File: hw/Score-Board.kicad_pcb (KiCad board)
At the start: 2 copper layers, 0 parts

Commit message: PCB routing done
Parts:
- added 5V: Conn_01x01, Connector_PinHeader_2.54mm:PinHeader_1x01_P2.54mm_Vertical, F.Cu at (151.0, 80.0)
- added BZ1: Buzzer, Buzzer_Beeper:Buzzer_12x9.5RM7.6, F.Cu at (133.2, 77.5)
- added C1: 10uF, Capacitor_THT:CP_Radial_D8.0mm_P3.50mm, F.Cu at (106.5, 113.1)
- added C2: 1.0uF, Capacitor_THT:CP_Radial_D5.0mm_P2.00mm, F.Cu at (140.3, 72.4)
- added C3: 1.0uF, Capacitor_THT:CP_Radial_D5.0mm_P2.00mm, F.Cu at (148.5, 72.4)
- added C4: 0.1uF, Capacitor_THT:CP_Radial_D5.0mm_P2.00mm, F.Cu at (217.8, 54.6)
- added C5: 0.1uF, Capacitor_THT:CP_Radial_D5.0mm_P2.00mm, F.Cu at (46.4, 54.6)
- added D1: 1N4004, Diode_THT:D_DO-41_SOD81_P10.16mm_Horizontal, F.Cu at (123.1, 90.2)
- added D2: D_Schottky_PP, Diode_THT:D_DO-35_SOD27_P10.16mm_Horizontal, F.Cu at (138.3, 90.2)
- added D3: D_Schottky, Diode_THT:D_DO-35_SOD27_P10.16mm_Horizontal, F.Cu at (130.7, 90.2)
- added D4: D_Schottky_PP, Diode_THT:D_DO-35_SOD27_P10.16mm_Horizontal, F.Cu at (146.0, 90.2)
- added Display: Conn_02x09_Odd_Even, Connector_PinHeader_2.54mm:PinHeader_2x09_P2.54mm_Vertical, F.Cu at (44.4, 80.0)
- added H1: MountingHole, MountingHole:MountingHole_3.2mm_M3, F.Cu at (46.9, 115.6)
- added H2: MountingHole, MountingHole:MountingHole_3.2mm_M3, F.Cu at (218.3, 115.6)
- added H3: MountingHole, MountingHole:MountingHole_3.2mm_M3, F.Cu at (46.9, 64.8)
- added H4: MountingHole, MountingHole:MountingHole_3.2mm_M3, F.Cu at (218.3, 64.8)
- added H5: MountingHole, MountingHole:MountingHole_3.2mm_M3, F.Cu at (106.6, 51.0)
- added H6: MountingHole, MountingHole:MountingHole_3.2mm_M3, F.Cu at (157.4, 51.0)
- added INPUT: INPUT-SW, AES_Library:SW_TL1100F160Q, B.Cu at (131.9, 57.4)
- added IR1: TSOP382xx, OptoDevice:Vishay_MINICAST-3Pin, B.Cu at (220.9, 47.0)
- added IR2: TSOP382xx, OptoDevice:Vishay_MINICAST-3Pin, B.Cu at (49.4, 47.0)
- added J-V12: J-V12, Connector_PinHeader_2.54mm:PinHeader_1x02_P2.54mm_Vertical, F.Cu at (115.5, 97.8)
- added J-V3.3: J-V3.3, Connector_PinHeader_2.54mm:PinHeader_1x02_P2.54mm_Vertical, F.Cu at (147.5, 103.9)
- added J-VSYS: J-VSYS, Connector_PinHeader_2.54mm:PinHeader_1x02_P2.54mm_Vertical, F.Cu at (155.9, 119.7)
- added J1: Barrel_Jack, AES_Library:CUI_PJ-037B, F.Cu at (132.0, 109.3)
- added J2: Screw_Terminal_01x02, TerminalBlock_Philmore:TerminalBlock_Philmore_TB132_1x02_P5.00mm_Horizontal, F.Cu at (116.7, 114.0)
- added J3: Conn_01x04, Connector_PinHeader_2.54mm:PinHeader_1x04_P2.54mm_Vertical, B.Cu at (128.1, 46.0)
- added J4: Conn_01x03, Connector_PinHeader_2.54mm:PinHeader_1x03_P2.54mm_Vertical, F.Cu at (215.8, 96.6)
- added J5: Conn_01x04, Connector_PinHeader_2.54mm:PinHeader_1x04_P2.54mm_Vertical, F.Cu at (156.1, 63.5)
- added PWR: LED, LED_THT:LED_D5.0mm, F.Cu at (146.0, 118.2)
- added Q1: 2N3904, Package_TO_SOT_THT:TO-92_Inline, F.Cu at (90.1, 51.5)
- added Q10: 2N3905, Package_TO_SOT_THT:TO-92_Inline, F.Cu at (84.7, 70.2)
- added Q11: 2N3905, Package_TO_SOT_THT:TO-92_Inline, F.Cu at (102.5, 82.9)
- added Q12: 2N3905, Package_TO_SOT_THT:TO-92_Inline, F.Cu at (84.7, 87.9)
- added Q13: 2N3905, Package_TO_SOT_THT:TO-92_Inline, F.Cu at (102.5, 100.6)
- added Q14: 2N3905, Package_TO_SOT_THT:TO-92_Inline, F.Cu at (84.7, 105.7)
- added Q15: 2N3904, Package_TO_SOT_THT:TO-92_Inline, F.Cu at (63.3, 50.8)
- added Q16: 2N3904, Package_TO_SOT_THT:TO-92_Inline, F.Cu at (73.8, 58.5)
- added Q17: 2N3904, Package_TO_SOT_THT:TO-92_Inline, F.Cu at (63.3, 68.6)
- added Q18: 2N3904, Package_TO_SOT_THT:TO-92_Inline, F.Cu at (73.8, 76.0)
- added Q19: 2N3904, Package_TO_SOT_THT:TO-92_Inline, F.Cu at (63.3, 86.4)
- added Q2: 2N3904, Package_TO_SOT_THT:TO-92_Inline, F.Cu at (107.9, 64.0)
- added Q20: 2N3904, Package_TO_SOT_THT:TO-92_Inline, F.Cu at (73.8, 94.0)
- added Q21: 2N3904, Package_TO_SOT_THT:TO-92_Inline, F.Cu at (63.3, 104.2)
- added Q22: 2N3904, Package_TO_SOT_THT:TO-92_Inline, F.Cu at (73.8, 111.8)
- added Q3: 2N3904, Package_TO_SOT_THT:TO-92_Inline, F.Cu at (90.1, 69.1)
- added Q4: 2N3904, Package_TO_SOT_THT:TO-92_Inline, F.Cu at (107.9, 81.8)
- added Q5: 2N3904, Package_TO_SOT_THT:TO-92_Inline, F.Cu at (90.1, 86.9)
- added Q6: 2N3904, Package_TO_SOT_THT:TO-92_Inline, F.Cu at (107.9, 99.6)
- added Q7: 2N3904, Package_TO_SOT_THT:TO-92_Inline, F.Cu at (90.1, 104.7)
- added Q8: 2N3905, Package_TO_SOT_THT:TO-92_Inline, F.Cu at (84.4, 52.4)
- added Q9: 2N3905, Package_TO_SOT_THT:TO-92_Inline, F.Cu at (102.5, 65.1)
- added R1: 150, Resistor_THT:R_Axial_DIN0207_L6.3mm_D2.5mm_P10.16mm_Horizontal, F.Cu at (205.7, 67.3)
- added R10: 1k, Resistor_THT:R_Axial_DIN0207_L6.3mm_D2.5mm_P10.16mm_Horizontal, F.Cu at (92.4, 75.5)
- added R11: 270, Resistor_THT:R_Axial_DIN0207_L6.3mm_D2.5mm_P10.16mm_Horizontal, F.Cu at (90.1, 64.8)
- added R12: 1k, Resistor_THT:R_Axial_DIN0207_L6.3mm_D2.5mm_P10.16mm_Horizontal, F.Cu at (110.1, 88.2)
- added R13: 270, Resistor_THT:R_Axial_DIN0207_L6.3mm_D2.5mm_P10.16mm_Horizontal, F.Cu at (107.9, 77.5)
- added R14: 1k, Resistor_THT:R_Axial_DIN0207_L6.3mm_D2.5mm_P10.16mm_Horizontal, F.Cu at (92.4, 93.3)
- added R15: 270, Resistor_THT:R_Axial_DIN0207_L6.3mm_D2.5mm_P10.16mm_Horizontal, F.Cu at (90.1, 82.6)
- added R16: 1k, Resistor_THT:R_Axial_DIN0207_L6.3mm_D2.5mm_P10.16mm_Horizontal, F.Cu at (110.1, 106.0)
- added R17: 270, Resistor_THT:R_Axial_DIN0207_L6.3mm_D2.5mm_P10.16mm_Horizontal, F.Cu at (107.9, 95.3)
- added R18: 1k, Resistor_THT:R_Axial_DIN0207_L6.3mm_D2.5mm_P10.16mm_Horizontal, F.Cu at (92.4, 111.0)
- added R19: 270, Resistor_THT:R_Axial_DIN0207_L6.3mm_D2.5mm_P10.16mm_Horizontal, F.Cu at (90.1, 100.4)
- added R2: 150, Resistor_THT:R_Axial_DIN0207_L6.3mm_D2.5mm_P10.16mm_Horizontal, F.Cu at (54.5, 62.3)
- added R20: 43, Resistor_THT:R_Axial_DIN0207_L6.3mm_D2.5mm_P10.16mm_Horizontal, F.Cu at (59.3, 57.1)
- added R3: 150, Resistor_THT:R_Axial_DIN0207_L6.3mm_D2.5mm_P10.16mm_Horizontal, F.Cu at (192.9, 54.6)
- added R33: 43, Resistor_THT:R_Axial_DIN0207_L6.3mm_D2.5mm_P10.16mm_Horizontal, F.Cu at (69.5, 62.3)
- added R34: 43, Resistor_THT:R_Axial_DIN0207_L6.3mm_D2.5mm_P10.16mm_Horizontal, F.Cu at (59.3, 74.8)
- added R39: 43, Resistor_THT:R_Axial_DIN0207_L6.3mm_D2.5mm_P10.16mm_Horizontal, F.Cu at (69.5, 80.0)
- added R4: 150, Resistor_THT:R_Axial_DIN0207_L6.3mm_D2.5mm_P10.16mm_Horizontal, F.Cu at (192.9, 57.2)
- added R40: 43, Resistor_THT:R_Axial_DIN0207_L6.3mm_D2.5mm_P10.16mm_Horizontal, F.Cu at (59.3, 92.6)
- added R41: 43, Resistor_THT:R_Axial_DIN0207_L6.3mm_D2.5mm_P10.16mm_Horizontal, F.Cu at (69.5, 97.8)
- added R42: 43, Resistor_THT:R_Axial_DIN0207_L6.3mm_D2.5mm_P10.16mm_Horizontal, F.Cu at (59.3, 110.4)
- added R43: 43, Resistor_THT:R_Axial_DIN0207_L6.3mm_D2.5mm_P10.16mm_Horizontal, F.Cu at (69.5, 115.6)
- added R5: 150, Resistor_THT:R_Axial_DIN0207_L6.3mm_D2.5mm_P10.16mm_Horizontal, F.Cu at (153.6, 110.8)
- added R6: 1k, Resistor_THT:R_Axial_DIN0207_L6.3mm_D2.5mm_P10.16mm_Horizontal, F.Cu at (92.0, 57.8)
- added R7: 270, Resistor_THT:R_Axial_DIN0207_L6.3mm_D2.5mm_P10.16mm_Horizontal, F.Cu at (90.1, 47.0)
- added R8: 1k, Resistor_THT:R_Axial_DIN0207_L6.3mm_D2.5mm_P10.16mm_Horizontal, F.Cu at (110.1, 70.4)
- added R9: 270, Resistor_THT:R_Axial_DIN0207_L6.3mm_D2.5mm_P10.16mm_Horizontal, F.Cu at (107.9, 59.7)
- added SD1: MicroSD-Socket, AES_Library:SDCard-GCT_MEM2075-00-140-01-A, F.Cu at (199.7, 118.6)
- added SW1: RESET, AES_Library:SW_TL1100F160Q, F.Cu at (199.3, 95.3)
- added SW2: NETWORK, AES_Library:SW_TL1100F160Q, F.Cu at (199.3, 76.2)
- added U1: PicoW, AES_Library:RPi_PicoW_SMD_TH, F.Cu at (175.2, 96.9)
- added U2: E18-MS1-PCB, AES_Library:E18-MS1-PCB-AES, F.Cu at (178.8, 43.9)
- added U5: MCP1702-5002E, Package_TO_SOT_THT:TO-92_Inline, F.Cu at (142.2, 80.0)
- added ZB-NET: LED, LED_THT:LED_D5.0mm, F.Cu at (200.7, 61.0)
- added ZB-RUN: LED, LED_THT:LED_D5.0mm, F.Cu at (200.7, 50.8)
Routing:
- net GND: track 0.00 -> 914.5 mm, vias 0 -> 1
- net +3.3V: track 0.00 -> 366.3 mm, vias 0 -> 3
- net +12V: track 0.00 -> 283.5 mm
- net /SE.B: track 0.00 -> 179.9 mm, vias 0 -> 2
- net /IR_2: track 0.00 -> 171.6 mm
- net /SE.C: track 0.00 -> 168.7 mm, vias 0 -> 2
- net /SE.D: track 0.00 -> 154.7 mm, vias 0 -> 2
- net /SE.G: track 0.00 -> 154.7 mm, vias 0 -> 1
- net /SE.F: track 0.00 -> 146.0 mm, vias 0 -> 2
- net /SE.E: track 0.00 -> 144.1 mm, vias 0 -> 3
- net /SE.A: track 0.00 -> 140.6 mm, vias 0 -> 1
- net /SE.P: track 0.00 -> 121.9 mm
- net /RESET: track 0.00 -> 113.6 mm, vias 0 -> 1
- net /I2C_SDA: track 0.00 -> 106.7 mm
- net /I2C_CLK: track 0.00 -> 105.7 mm
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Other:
- board outline added: 184.2 x 81.3 mm
- board text added: "+"
- board text added: "3.3"
- board text added: "CLK"
- board text added: "FAN"
- board text added: "GND"
- board text added: "I2C"
- board text added: "RX"
- board text added: "SDA"
- board text added: "SERIAL"
- board text added: "TX"
- board text added: "Wi-Fi"
- board text added: "ZB-I2C"
- board text added: "locked"

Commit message: Add pull-down res to segment drives.
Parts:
- added G***: LOGO, AES_Library:SILKY-DESIGN-logo-0_50-AES, F.Cu at (59.5, 115.7)
- added G***: LOGO, AES_Library:SILKY-DESIGN-logo-0_50-AES, B.Cu at (178.7, 46.9)
- added R21: 10k, Resistor_THT:R_Axial_DIN0207_L6.3mm_D2.5mm_P10.16mm_Horizontal, F.Cu at (64.7, 55.9)
- added R22: 10k, Resistor_THT:R_Axial_DIN0207_L6.3mm_D2.5mm_P10.16mm_Horizontal, F.Cu at (53.2, 72.4)
- added R23: 10k, Resistor_THT:R_Axial_DIN0207_L6.3mm_D2.5mm_P10.16mm_Horizontal, F.Cu at (63.3, 78.5)
- added R24: 10k, Resistor_THT:R_Axial_DIN0207_L6.3mm_D2.5mm_P10.16mm_Horizontal, F.Cu at (73.8, 72.4)
- added R25: 10k, Resistor_THT:R_Axial_DIN0207_L6.3mm_D2.5mm_P10.16mm_Horizontal, F.Cu at (63.3, 92.6)
- added R26: 10k, Resistor_THT:R_Axial_DIN0207_L6.3mm_D2.5mm_P10.16mm_Horizontal, F.Cu at (78.7, 96.4)
- added R27: 10k, Resistor_THT:R_Axial_DIN0207_L6.3mm_D2.5mm_P10.16mm_Horizontal, F.Cu at (77.9, 116.6)
- added R28: 10k, Resistor_THT:R_Axial_DIN0207_L6.3mm_D2.5mm_P10.16mm_Horizontal, F.Cu at (73.8, 107.5)
- IR1: moved to F.Cu
- R20, R33, R34, R39, R40, R41, R42, R43: value 43 -> 47
- moved IR1 5.08 mm to (215.8, 47.0), turned to 0 degrees
- moved Q21 2.79 mm to (63.3, 107.0)
- moved Q18 2.29 mm to (73.8, 78.3)
- moved R39 2.29 mm to (69.5, 82.3)
- moved Q22 1.40 mm to (73.8, 113.2)
- turned LED1 to 180 degrees
- renumbered Display to Conn1, INPUT to INPUT1, J-V3.3 to J6, J-V12 to J7, J-VSYS to J8, PWR to LED1, ZB-RUN to LED2, ZB-NET to LED3, 5V to TP1
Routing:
- net GND: track 914.5 -> 958.1 mm
- net /SD.B: track 42.3 -> 17.1 mm
- net /SD.G: track 22.5 -> 42.4 mm
- net /DD.IND: track 62.2 -> 44.5 mm
- net /SD.F: track 31.9 -> 39.4 mm
- net /SE.G: track 154.7 -> 151.2 mm
- net /SD.C: track 26.7 -> 30.1 mm
- net /SD.P: track 35.1 -> 38.4 mm
- net Net-(Q21-E): track 12.6 -> 10.1 mm
- net /SD.D: track 36.4 -> 38.8 mm
- net /IR_1: track 60.2 -> 58.1 mm
- net /VIR.A: track 18.8 -> 20.9 mm
- net Net-(LED1-A): track 6.13 -> 7.62 mm
- net /SE.E: track 144.1 -> 142.9 mm
- net /SD.A: track 38.1 -> 39.3 mm
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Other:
- outline, holes or cut-outs redrawn
- board text added: "Scoreboard - Main V1.0 Copyright AESilky 2023"

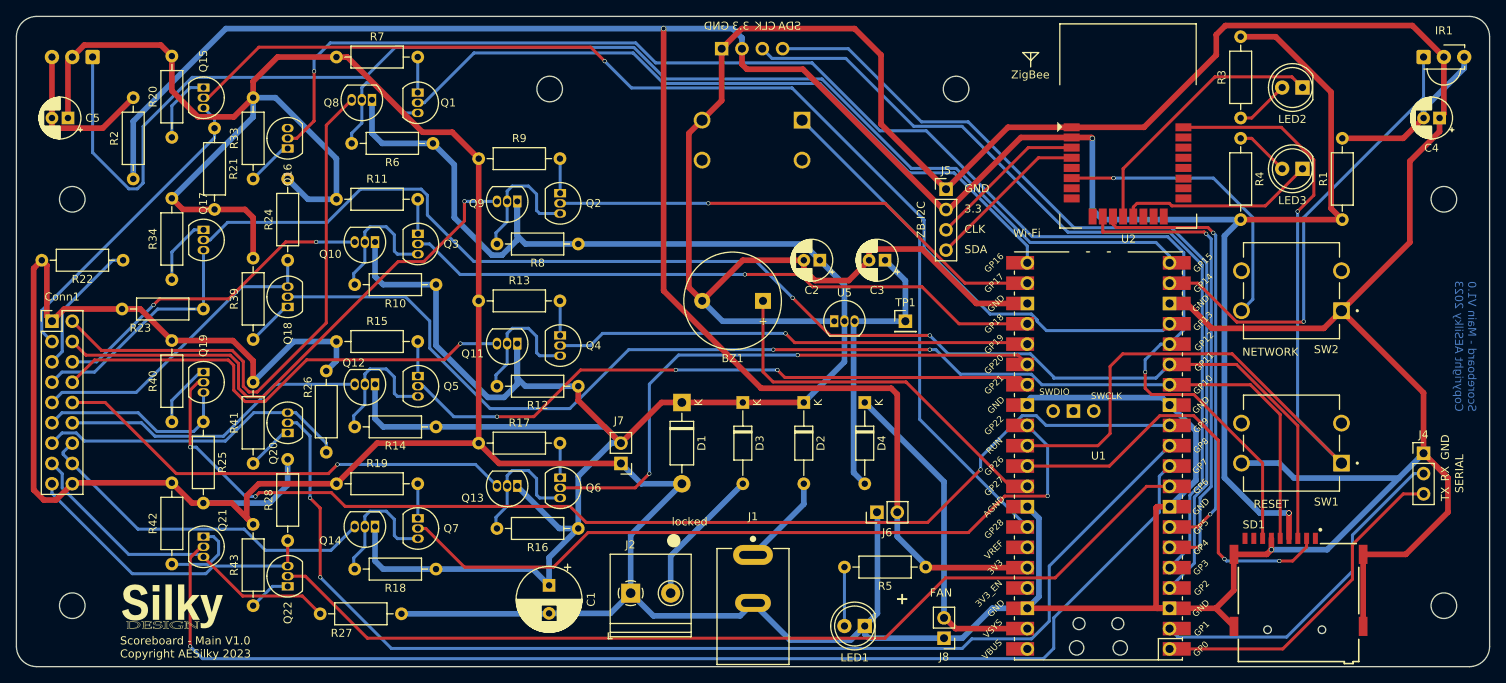
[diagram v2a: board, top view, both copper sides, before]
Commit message: SPI for display & SD, Seg&Dig enables 16 straight GPIOs.
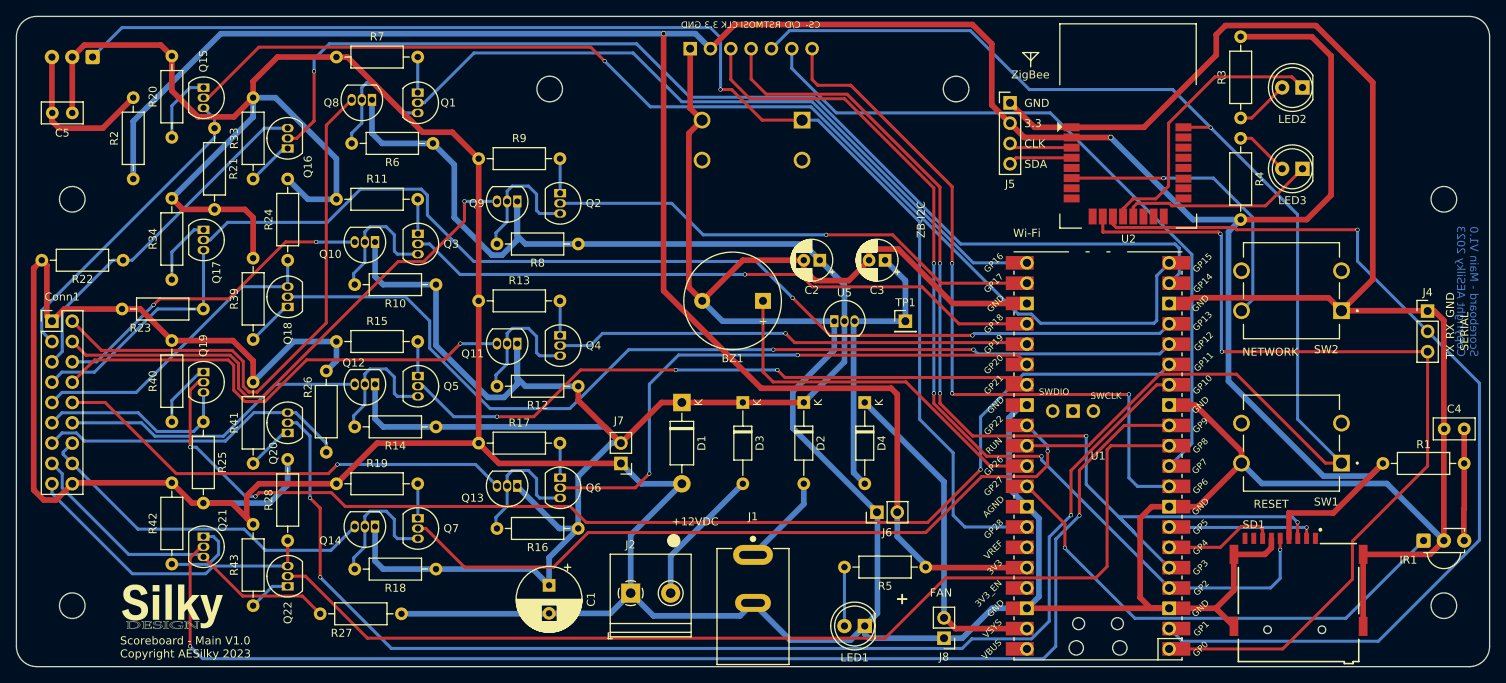
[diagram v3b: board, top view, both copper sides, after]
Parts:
- C4, C5: footprint Capacitor_THT:CP_Radial_D5.0mm_P2.00mm -> Capacitor_THT:C_Disc_D5.0mm_W2.5mm_P2.50mm
- J3: value Conn_01x04 -> SPI-Disp; footprint Connector_PinHeader_2.54mm:PinHeader_1x04_P2.54mm_Vertical -> Connector_PinSocket_2.54mm:PinSocket_1x07_P2.54mm_Vertical
- LED1: value LED -> PWR
- LED2: value LED -> ZBRUN
- LED3: value LED -> ZBNWRK
- moved IR1 60.4 mm to (215.8, 107.5)
- moved C4 38.9 mm to (218.4, 93.5), turned to 0 degrees
- moved R1 30.9 mm to (210.7, 97.8), turned to 0 degrees
- moved J4 17.8 mm to (216.3, 78.8)
- moved J5 13.4 mm to (164.1, 52.8)
- moved J3 3.94 mm to (124.1, 46.0)
- moved C5 0.83 mm to (46.9, 54.0)
- moved U1 0.05 mm to (175.1, 96.9)
- renumbered INPUT1 to SW3
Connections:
- J3 pad 3: /I2C_CLK -> /SPICK
- J3 pad 4: /I2C_SDA -> /SPIMO
- J4 pad 2: /SC_RX -> /ZRX
- J4 pad 3: /SC_TX -> /ZTX
- SD1 pad 3: /SE.C -> /SPIMO
- SD1 pad 5: /SE.D -> /SPICK
- SD1 pad 7: /SE.B -> /SPIMI
- SW3 pad 1: /SW_IN -> /IR_2
- U1 pad 1: /SC_TX -> /ZTX
- U1 pad 10: /SE.G -> /DISP_CD
- U1 pad 11: /SE.F -> /SE.P
- U1 pad 12: /SE.E -> /SE.G
- U1 pad 14: /SE.D -> /SE.F
- U1 pad 15: /SE.C -> /SE.E
- U1 pad 16: /SE.B -> /SE.D
- U1 pad 17: /SE.A -> /SE.C
- U1 pad 19: /IR_1 -> /SE.B
- U1 pad 2: /SC_RX -> /ZRX
- U1 pad 20: /IR_2 -> /SE.A
- U1 pad 31: /CARD_CS- -> /BZR
- U1 pad 32: /BZR -> /IR_1
- U1 pad 34: /SW_IN -> /IR_2
- U1 pad 4: /I2C_SDA -> /SPICK
- U1 pad 5: /I2C_CLK -> /SPIMO
- U1 pad 6: /ZTX -> /SPIMI
- U1 pad 7: /ZRX -> /CARD_CS-
- U1 pad 9: /SE.P -> /DISP_CS-
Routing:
- net /SPIMO: track 0.00 -> 128.1 mm, vias 0 -> 4
- net /SPICK: track 0.00 -> 120.4 mm, vias 0 -> 4
- net /I2C_SDA: track 106.7 -> 0.00 mm
- net /I2C_CLK: track 105.7 -> 0.00 mm
- net /DISP_CS-: track 0.00 -> 90.9 mm, vias 0 -> 3
- net /DISP_CD: track 0.00 -> 89.7 mm
- net /ZRX: track 55.3 -> 121.6 mm, vias 2 -> 1
- net /SW_IN: track 62.5 -> 0.00 mm
- net /ZTX: track 58.8 -> 116.1 mm
- net /RESET: track 113.6 -> 160.6 mm
- net /SE.B: track 179.9 -> 136.3 mm, vias 2 -> 1
- net /SC_RX: track 43.3 -> 0.00 mm
- net /SC_TX: track 42.3 -> 0.00 mm
- net GND: track 958.1 -> 919.8 mm, vias 1 -> 0
- net /CARD_CS-: track 55.1 -> 18.5 mm, vias 2 -> 1
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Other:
- board text added: "+12VDC"
- board text added: "C/D"
- board text added: "CS-"
- board text added: "MOSI"
- board text added: "RST"
- board text removed: "I2C"
- board text removed: "locked"
